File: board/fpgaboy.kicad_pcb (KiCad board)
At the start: 4 copper layers, 50 x 50 mm, 87 parts, among them J1 Conn_01x12, J2 Conn_01x06, J3 Micro_SD_Card_Det, J4 Conn_01x06, P1 ILI9341, P2 CONN_01X02, P3 USB_OTG, Q1 BSS816NW, SW1 SWITCH_SPST, U1 iCE40-HX8k-BG121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

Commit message: Continue BGA escape. Pin-swap LCD and uSD card so that the traces don't have to cross.
Former-commit-id: f8ac038b637c7257d92a3d2f030f50e78c9c9bc2 [formerly 6bcc831231e3fdf82be743b82d14a98c5b81e0ac]
Former-commit-id: 605b2bd4fd829a74481d758a2aba6bf016992be6
Former-commit-id: 63a570fdaa14407f687558ae361da6e3eddfbbe5
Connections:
- U1 pad B11: /LCD_SDO -> /uSD_CLK
- U1 pad C11: /LCD_SDA -> /uSD_CMD
- U1 pad D10: /LCD_CS -> /uSD_DAT3
- U1 pad D11: /LCD_D/C -> /uSD_DAT2
- U1 pad D9: /LCD_RESET -> /uSD_DAT0
- U1 pad E11: /LCD_SCL -> /uSD_DAT1
- U1 pad E8: /LCD_PWM -> Net-(U1-PadE8)
- U1 pad G10: /uSD_CMD -> /LCD_SDO
- U1 pad G8: /uSD_DAT2 -> /LCD_CS
- U1 pad G9: /uSD_CLK -> Net-(U1-PadG9)
- U1 pad H10: /uSD_DAT0 -> /LCD_SCL
- U1 pad H11: /uSD_DAT3 -> /LCD_SDA
- U1 pad J10: /uSD_DAT1 -> /LCD_D/C
- U1 pad J11: Net-(U1-PadJ11) -> /LCD_PWM
- U1 pad K11: Net-(U1-PadK11) -> /LCD_RESET
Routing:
- net /uSD_CLK: track 0.00 -> 2.37 mm
- net /LCD_SDO: track 2.37 -> 0.00 mm
- net /uSD_CMD: track 0.00 -> 1.97 mm
- net /LCD_SDA: track 1.97 -> 0.00 mm
- net /uSD_DAT1: track 0.00 -> 1.28 mm
- net /LCD_SCL: track 1.28 -> 0.00 mm

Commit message: .
Former-commit-id: 099437aeaa0f87b81eeb045cc0cc2065e57b2218 [formerly 5b995d2ac2d80979005ea056349abce62d091246]
Former-commit-id: e3da0e3630d2230d9d68ed8e3ef45ab7c693987d
Former-commit-id: aab129dfe919954ae2f0a219e0799318124eaf7d
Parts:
- moved C3 3.00 mm to (169.5, 104.5)
- moved R7 3.00 mm to (169.5, 106.0)
- moved U2 2.40 mm to (169.5, 108.0)
- moved C4 1.22 mm to (172.0, 108.0)
- moved C9 0.50 mm to (169.5, 110.0)
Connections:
- RN1 pad 1: /FPGA_UART_TX -> /uSD_DAT1
- RN1 pad 2: /FPGA_UART_RX -> /uSD_DAT0
- RN1 pad 3: /uSD_DAT2 -> /FPGA_UART_TX
- RN1 pad 4: /uSD_DAT3 -> /FPGA_UART_RX
- RN2 pad 1: /uSD_CMD -> /uSD_CLK
- RN2 pad 2: /uSD_CLK -> /uSD_CMD
- RN2 pad 3: /uSD_DAT0 -> /uSD_DAT2
- RN2 pad 4: /uSD_DAT1 -> /uSD_DAT3
- U1 pad G1: Net-(U1-PadG1) -> /SRAM_DQ10
- U1 pad H9: /SRAM_DQ10 -> Net-(U1-PadH9)
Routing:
- net /LCD_SDO: track 0.00 -> 15.7 mm
- net /LCD_SDA: track 0.00 -> 12.7 mm
- net /LCD_SCL: track 0.00 -> 12.3 mm
- net /LCD_PWM: track 0.00 -> 11.0 mm
- net /LCD_RESET: track 0.00 -> 10.3 mm
- net /uSD_DAT0: track 0.00 -> 6.45 mm
- net /VCCPLL0: track 0.57 -> 6.92 mm, vias 1 -> 0
- net /uSD_DAT3: track 0.00 -> 5.19 mm
- net /uSD_DAT2: track 0.00 -> 4.28 mm
- net /FPGA_CFG_SO: track 0.00 -> 3.77 mm
- net /SRAM_DQ6: track 2.50 -> 5.93 mm
- net /FPGA_CFG_~SS: track 0.00 -> 3.15 mm
- net Net-(C3-Pad2): track 0.00 -> 2.92 mm
- net /uSD_DAT1: track 1.28 -> 4.18 mm
- net /FPGA_CFG_DONE: track 0.00 -> 2.60 mm
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
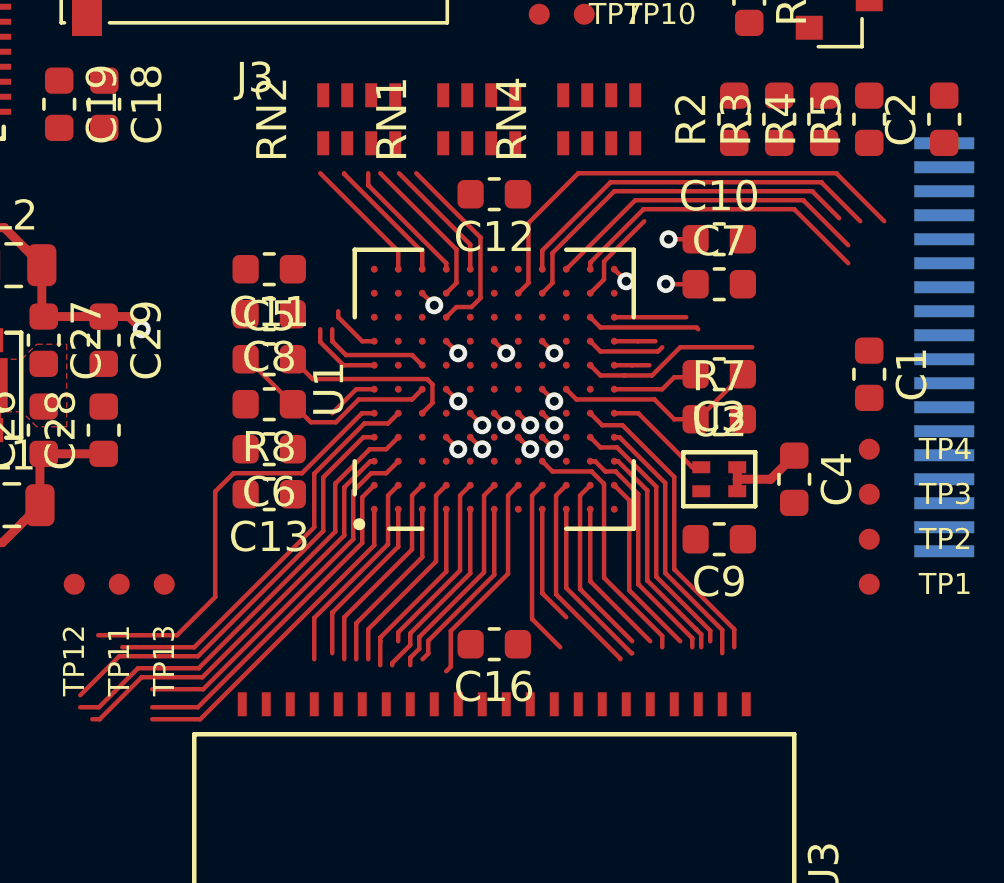
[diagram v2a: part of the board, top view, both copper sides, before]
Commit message: BGA route out 99%. Use a gbin for an SRAM pin to avoid nasty route-out.
Former-commit-id: 07f92fcfe0b8196dbaa0211e318f2cb0094c4f09 [formerly 87ade9239a6d7c42a9d86e2b403b5dd729dbe203]
Former-commit-id: 3d668f6e0e5d229a5cfefa9fffbb2161422c9dee
Former-commit-id: 99b8390e32f2fc2be4ea2818cc2b91bb5d9c6d22
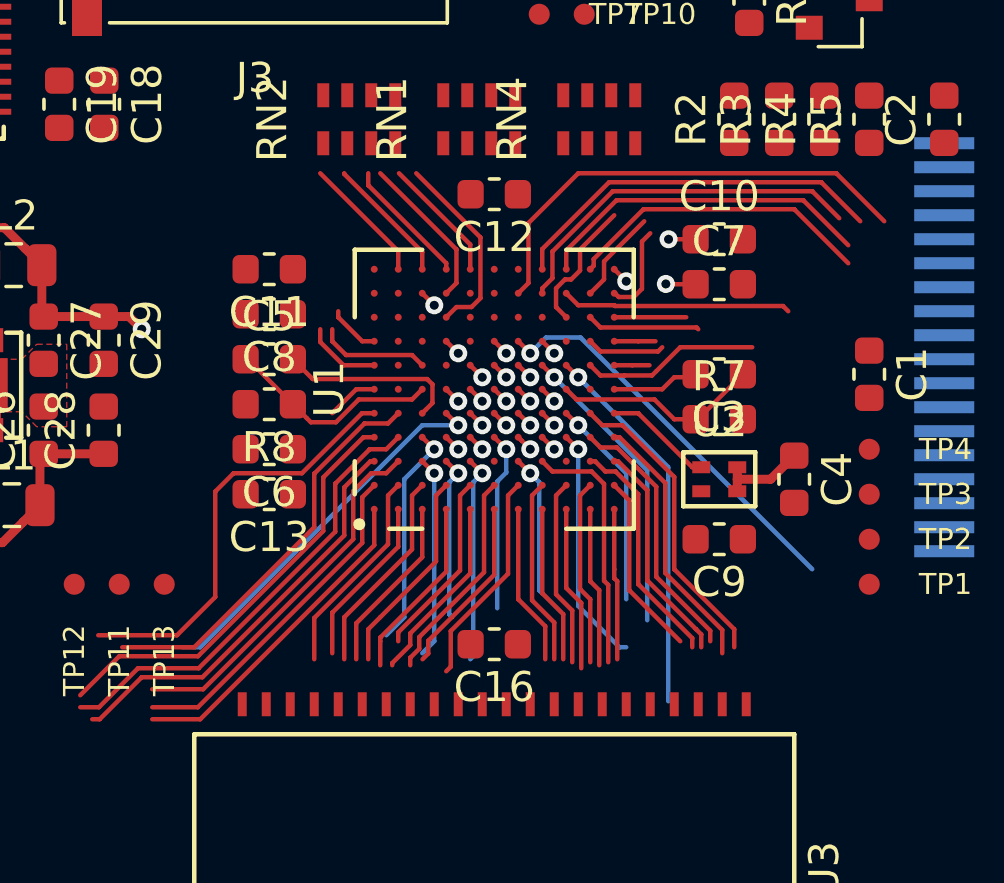
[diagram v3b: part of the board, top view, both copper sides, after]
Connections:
- U1 pad J8: /SRAM_DQ7 -> Net-(U1-PadJ8)
- U1 pad L1: Net-(U1-PadL1) -> /SRAM_DQ7
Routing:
- net /LCD_CS: track 0.00 -> 13.4 mm, vias 0 -> 1
- net /GPIO_SW4: track 0.00 -> 12.8 mm, vias 0 -> 1
- net /SRAM_DQ4: track 0.00 -> 12.6 mm, vias 0 -> 1
- net /SRAM_DQ5: track 0.00 -> 9.95 mm, vias 0 -> 1
- net /SRAM_~OE: track 0.00 -> 7.96 mm, vias 0 -> 1
- net /LCD_D/C: track 0.00 -> 7.65 mm
- net /SRAM_DQ13: track 0.00 -> 7.43 mm, vias 0 -> 1
- net /SRAM_DQ2: track 0.00 -> 7.03 mm, vias 0 -> 1
- net /SRAM_A5: track 0.00 -> 6.93 mm, vias 0 -> 1
- net /SRAM_DQ14: track 0.00 -> 6.73 mm, vias 0 -> 1
- net /SRAM_A8: track 0.00 -> 5.99 mm, vias 0 -> 1
- net /SRAM_A10: track 0.00 -> 5.58 mm, vias 0 -> 1
- net /SRAM_A3: track 0.00 -> 5.53 mm, vias 0 -> 1
- net /SRAM_DQ10: track 0.00 -> 5.37 mm
- net /SRAM_DQ7: track 0.00 -> 5.04 mm
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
